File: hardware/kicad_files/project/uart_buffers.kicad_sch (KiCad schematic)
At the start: 5 parts, among them J2 Conn_01x02_Socket, U10 SN74LVC1G125DCKR, U9 SN74LVC1G125DCKR

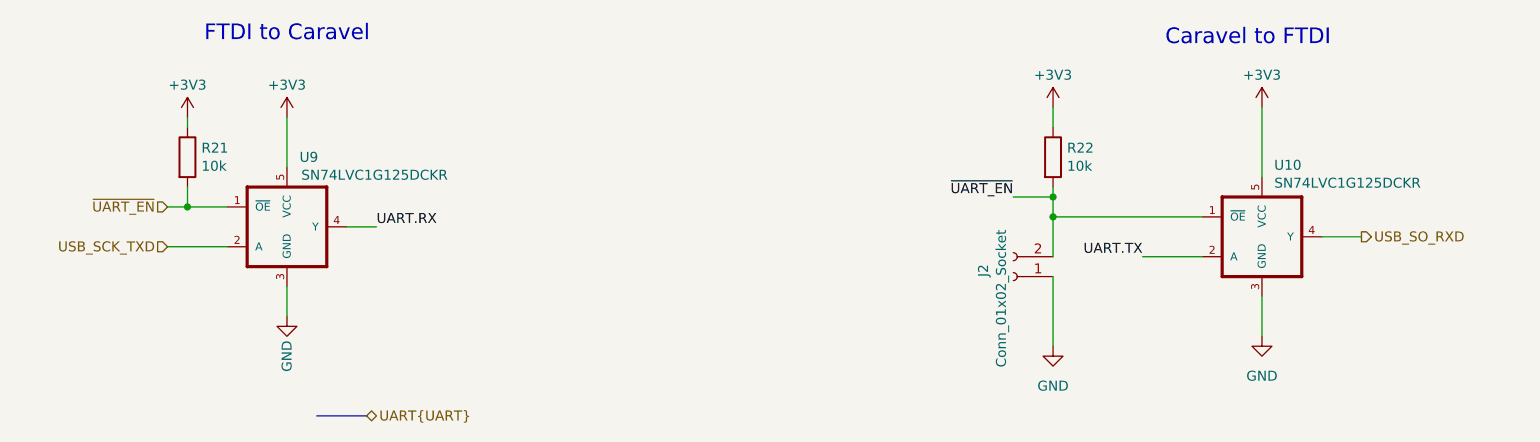
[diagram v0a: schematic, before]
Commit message: feat: optimize layout, reassign annotations, add 2x4 header for UART selection
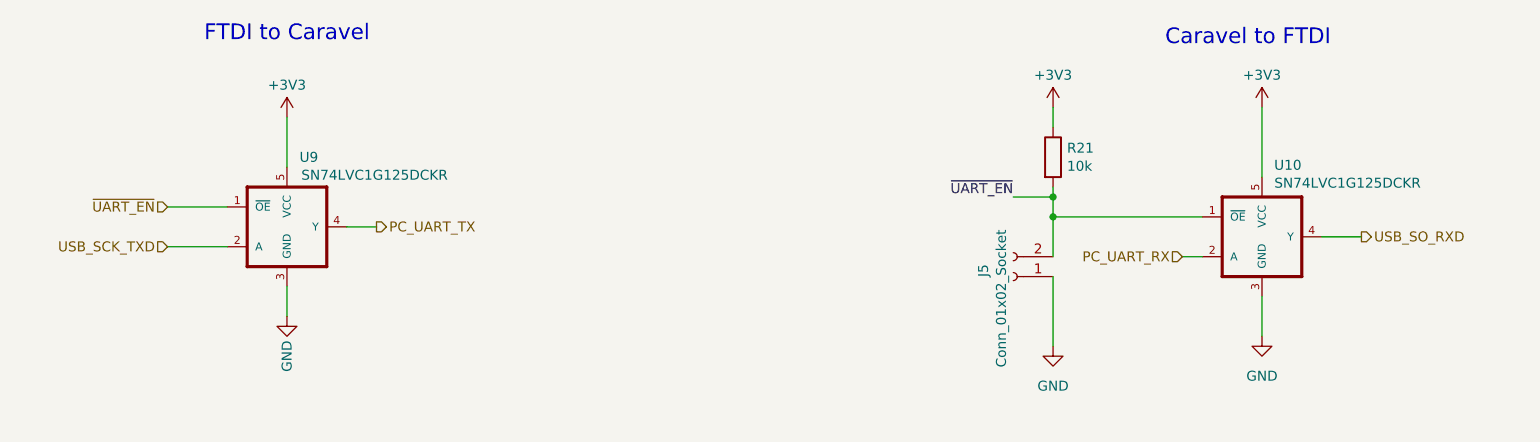
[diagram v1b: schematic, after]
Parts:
- removed R21: 10k, Resistor_SMD:R_0805_2012Metric, symbol Device:R
- renumbered J2 to J5, R22 to R21
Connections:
- net UART.RX renamed PC_UART_TX
- net UART.TX renamed PC_UART_RX

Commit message: feat: Implement all findings of the second review
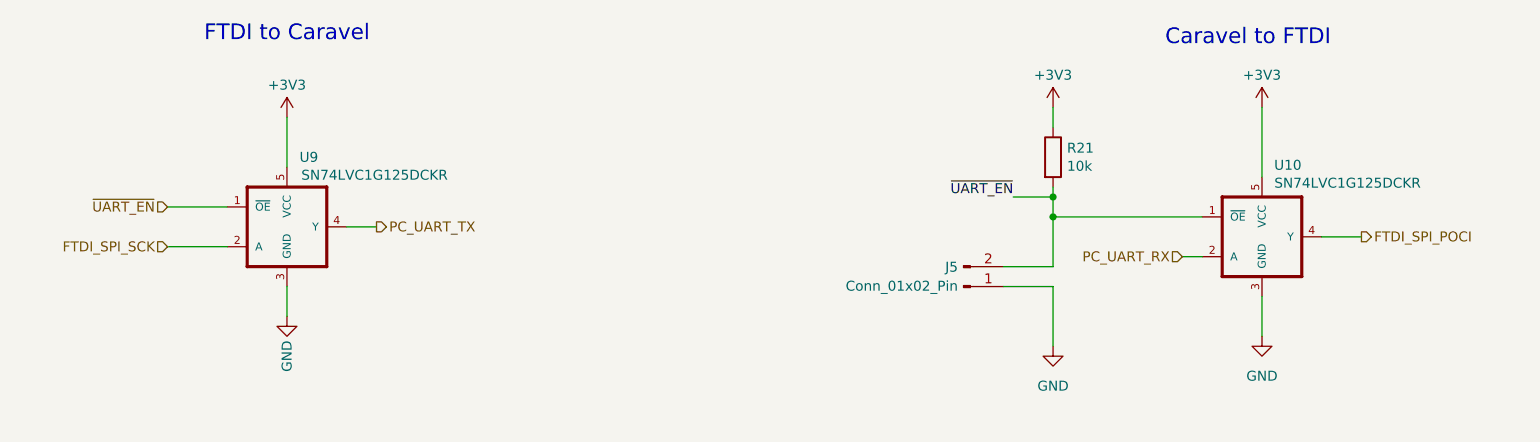
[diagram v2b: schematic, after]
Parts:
- removed J5: Conn_01x02_Socket, Connector_PinSocket_2.54mm:PinSocket_1x02_P2.54mm_Vertical, symbol Connector:Conn_01x02_Socket
- added J5: Conn_01x02_Pin, Connector_PinHeader_2.54mm:PinHeader_1x02_P2.54mm_Vertical, symbol Connector:Conn_01x02_Pin
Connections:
- net GND: now also J5.1 (Pin_1)
- net ~{UART_EN}: now also J5.2 (Pin_2)
- net USB_SCK_TXD renamed FTDI_SPI_SCK
- net USB_SO_RXD renamed FTDI_SPI_POCI
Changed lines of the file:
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@@
 	(wire
 		(pts
-			(xy 190.5 110.49) (xy 190.5 101.6)
+			(xy 190.5 110.49) (xy 190.5 102.87)
 		)
 		(stroke
@@
 	(wire
 		(pts
+			(xy 184.15 102.87) (xy 190.5 102.87)
+		)
+		(stroke
+			(width 0)
+			(type default)
+		)
+	)
+	(wire
+		(pts
+			(xy 184.15 100.33) (xy 190.5 100.33)
+		)
+		(stroke
+			(width 0)
+			(type default)
+		)
+	)
+	(wire
+		(pts
 			(xy 92.71 81.28) (xy 92.71 87.63)
 		)
@@
 	(wire
 		(pts
-			(xy 190.5 93.98) (xy 190.5 99.06)
+			(xy 190.5 93.98) (xy 190.5 100.33)
 		)
 		(stroke
@@
 		)
 	)
-	(hierarchical_label "USB_SCK_TXD"
+	(hierarchical_label "FTDI_SPI_SCK"
 		(shape input)
 		(at 77.47 97.79 180)
@@
 		)
 	)
-	(hierarchical_label "USB_SO_RXD"
+	(hierarchical_label "FTDI_SPI_POCI"
 		(shape output)
 		(at 229.87 96.52 0)
@@
 	)
 	(symbol
-		(lib_id "Connector:Conn_01x02_Socket")
-		(at 185.42 101.6 180)
-		(unit 1)
-		(exclude_from_sim no)
-		(in_bom yes)
-		(on_board yes)
-		(dnp no)
-		(property "Reference" "J5"
-			(at 181.61 100.838 90)
-			(effects
-				(font
-					(size 1.27 1.27)
-				)
-			)
-		)
-		(property "Value" "Conn_01x02_Socket"
-			(at 183.896 104.394 90)
-			(effects
-				(font
-					(size 1.27 1.27)
-				)
-			)
-		)
-		(property "Footprint" "Connector_PinSocket_2.54mm:PinSocket_1x02_P2.54mm_Vertical"
-			(at 185.42 101.6 0)
-			(effects
-				(font
-					(size 1.27 1.27)
-				)
-				(hide yes)
-			)
-		)
-		(property "Datasheet" "~"
-			(at 185.42 101.6 0)
-			(effects
-				(font
-					(size 1.27 1.27)
-				)
-				(hide yes)
-			)
-		)
-		(property "Description" "Generic connector, single row, 01x02, script generated"
-			(at 185.42 101.6 0)
-			(effects
-				(font
-					(size 1.27 1.27)
-				)
-				(hide yes)
-			)
-		)
-		(pin "1"
-		)
-		(pin "2"
-		)
-		(instances
-			(project "FABulous_board"
-				(path "/5664f05e-a3ef-4177-8026-c4580fa32c71/4820c043-623b-447e-8e47-990cd78f4dc2"
-					(reference "J5")
-					(unit 1)
-				)
-			)
-		)
-	)
-	(symbol
 		(lib_id "power:+3V3")
 		(at 92.71 81.28 0)
@@
 					(unit 1)
 				)
+			)
+		)
+	)
+	(symbol
+		(lib_id "Connector:Conn_01x02_Pin")
+		(at 179.07 102.87 0)
+		(mirror x)
+		(unit 1)
+		(exclude_from_sim no)
+		(in_bom yes)
+		(on_board yes)
+		(dnp no)
+		(fields_autoplaced yes)
+		(property "Reference" "J5"
+			(at 178.3589 100.3878 0)
+			(effects
+				(font
+					(size 1.27 1.27)
+				)
+				(justify right)
+			)
+		)
+		(property "Value" "Conn_01x02_Pin"
+			(at 178.3589 102.8121 0)
+			(effects
+				(font
+					(size 1.27 1.27)
+				)
+				(justify right)
+			)
+		)
+		(property "Footprint" "Connector_PinHeader_2.54mm:PinHeader_1x02_P2.54mm_Vertical"
+			(at 179.07 102.87 0)
+			(effects
+				(font
+					(size 1.27 1.27)
+				)
+				(hide yes)
+			)
+		)
+		(property "Datasheet" "~"
+			(at 179.07 102.87 0)
+			(effects
+				(font
+					(size 1.27 1.27)
+				)
+				(hide yes)
+			)
+		)
+		(property "Description" "Generic connector, single row, 01x02, script generated"
+			(at 179.07 102.87 0)
+			(effects
+				(font
+					(size 1.27 1.27)
+				)
+				(hide yes)
+			)
+		)
+		(pin "2"
+		)
+		(pin "1"
+		)
+		(instances
+			(project ""
+				(path "/5664f05e-a3ef-4177-8026-c4580fa32c71/4820c043-623b-447e-8e47-990cd78f4dc2"
+					(reference "J5")
+					(unit 1)
+				)

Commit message: fix: replace all local symbols and footprints with versions from KiCad or project libraries
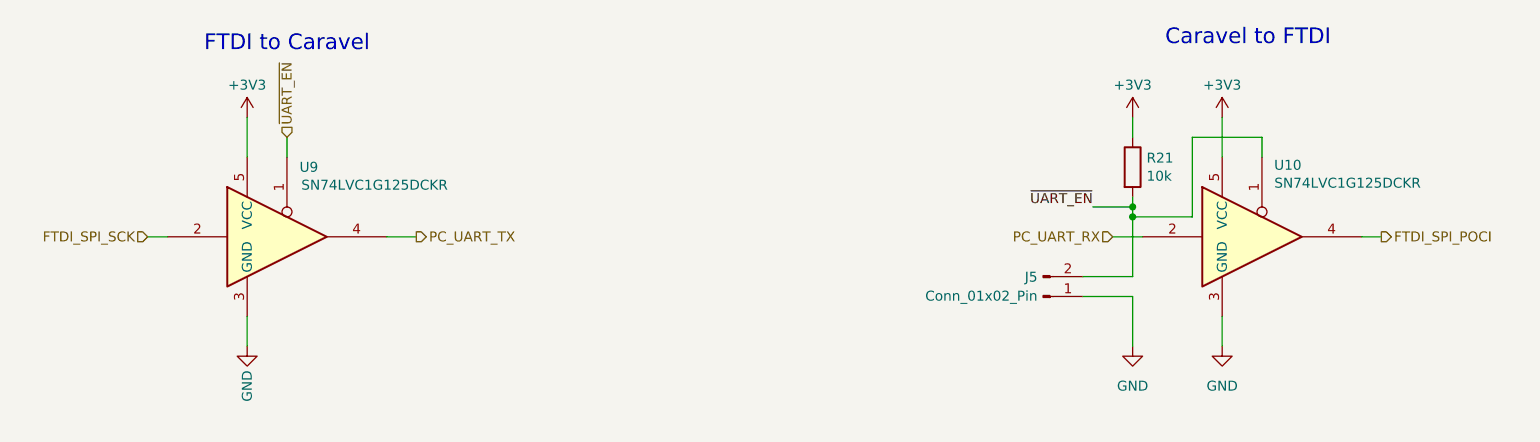
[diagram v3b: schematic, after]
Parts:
- U10, U9: footprint strive_foot_prints:SOT65P210X110-5N -> Package_TO_SOT_SMD:Texas_R-PDSO-G5_DCK-5; symbol Caravel_board:SN74LVC1G125DCKR -> 74xGxx:SN74LVC1G125DCK
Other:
- moved on the sheet: J5, R21
